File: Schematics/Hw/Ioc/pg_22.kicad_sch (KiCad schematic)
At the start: 8 parts, among them U2301 8641, U2302 8641, U2303 8641, U2304 8641, U2305 8641, U2306 8641, U2307 F04, U2308 F51

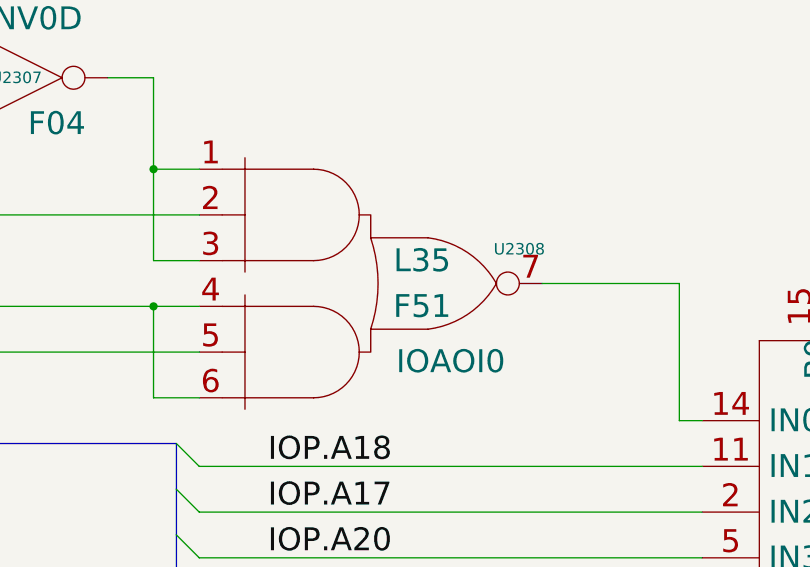
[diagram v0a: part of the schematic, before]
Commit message: Upgrade to KiCad9
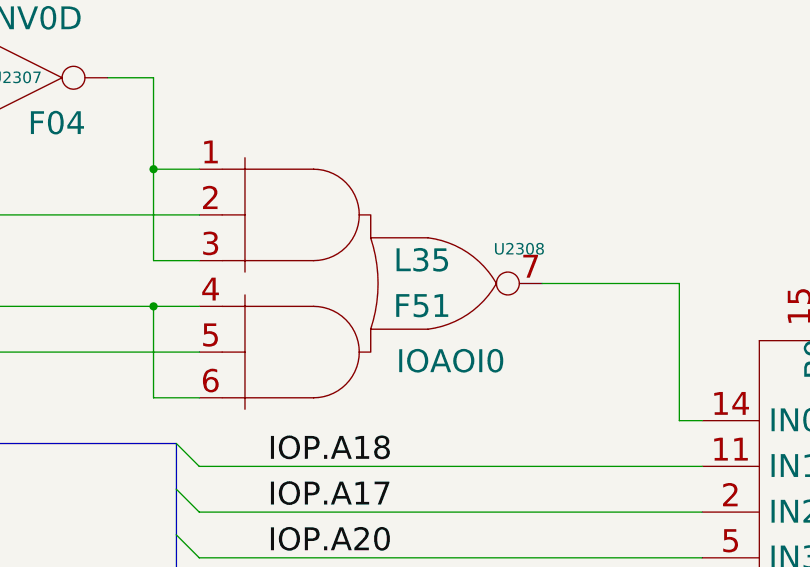
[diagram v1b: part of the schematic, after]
